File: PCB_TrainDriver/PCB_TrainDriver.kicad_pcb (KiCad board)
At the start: 2 copper layers, 1 part, among them Q1 BSC014N04LS

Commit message: Finished sch
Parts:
- added C1: 1uF 25V, Capacitor_SMD:C_0805_2012Metric, F.Cu at (166.2, 71.7)
- added C10: 1uF 25V, Capacitor_SMD:C_0805_2012Metric, F.Cu at (166.2, 86.7)
- added C11: 1000uF 35V, Capacitor_SMD:CP_Elec_10x10, F.Cu at (148.5, 103.0)
- added C12: 0.1uF 50V, Capacitor_SMD:C_0805_2012Metric, F.Cu at (166.2, 89.7)
- added C13: 1uF 25V, Capacitor_SMD:C_0805_2012Metric, F.Cu at (166.2, 92.7)
- added C14: 1000uF 35V, Capacitor_SMD:CP_Elec_10x10, F.Cu at (148.5, 114.9)
- added C15: 0.1uF, Capacitor_SMD:C_0402_1005Metric, F.Cu at (242.8, 50.7)
- added C16: 0.1uF, Capacitor_SMD:C_0402_1005Metric, F.Cu at (242.8, 52.7)
- added C17: 0.1uF, Capacitor_SMD:C_0402_1005Metric, F.Cu at (242.8, 54.6)
- added C18: 0.1uF, Capacitor_SMD:C_0402_1005Metric, F.Cu at (242.8, 56.6)
- added C19: 10uF, Capacitor_SMD:C_0402_1005Metric, F.Cu at (242.8, 58.6)
- added C2: 0.1uF 50V, Capacitor_SMD:C_0805_2012Metric, F.Cu at (166.2, 74.7)
- added C20: 10uF, Capacitor_SMD:C_1206_3216Metric, F.Cu at (224.8, 118.9)
- added C21: 0.1uF, Capacitor_SMD:C_0603_1608Metric, F.Cu at (212.6, 133.4)
- added C22: 33nF, Capacitor_SMD:C_0402_1005Metric, F.Cu at (216.8, 118.2)
- added C23: 18pF, Capacitor_SMD:C_0402_1005Metric, F.Cu at (216.8, 120.2)
- added C24: 47uF, Capacitor_SMD:C_1206_3216Metric, F.Cu at (224.8, 122.2)
- added C25: 0.1uF, Capacitor_SMD:C_0402_1005Metric, F.Cu at (216.8, 122.1)
- added C26: 1uF, Capacitor_SMD:C_0402_1005Metric, F.Cu at (216.8, 124.1)
- added C27: 220uF, Capacitor_SMD:C_1206_3216Metric, F.Cu at (224.8, 125.6)
- added C28: 0.1uF, Capacitor_SMD:C_0402_1005Metric, F.Cu at (216.8, 126.1)
- added C29: 0.1uF, Capacitor_SMD:C_0402_1005Metric, F.Cu at (242.8, 60.5)
- added C3: 1uF 25V, Capacitor_SMD:C_0805_2012Metric, F.Cu at (166.2, 77.7)
- added C30: 1uF, Capacitor_SMD:C_0402_1005Metric, F.Cu at (242.8, 62.5)
- added C31: 1uF, Capacitor_SMD:C_0402_1005Metric, F.Cu at (216.8, 128.1)
- added C32: 0.1uF, Capacitor_SMD:C_0402_1005Metric, F.Cu at (216.8, 130.0)
- added C4: 1uF 25V, Capacitor_SMD:C_0805_2012Metric, F.Cu at (166.2, 80.7)
- added C5: 1000uF 35V, Capacitor_SMD:CP_Elec_10x10, F.Cu at (148.5, 55.6)
- added C6: 1000uF 35V, Capacitor_SMD:CP_Elec_10x10, F.Cu at (148.5, 67.5)
- added C7: 1000uF 35V, Capacitor_SMD:CP_Elec_10x10, F.Cu at (148.5, 79.3)
- added C8: 1000uF 35V, Capacitor_SMD:CP_Elec_10x10, F.Cu at (148.5, 91.2)
- added C9: 1uF 25V, Capacitor_SMD:C_0805_2012Metric, F.Cu at (166.2, 83.7)
- added CN1: XT90PW-M.G.Y, Sharing_Footprint:CONN-TH_XT90PW-M.G.Y, F.Cu at (86.2, 76.9)
- added D1: SS34, Diode_SMD:D_SMA, F.Cu at (158.0, 142.0)
- added D2: SS34, Diode_SMD:D_SMA, F.Cu at (158.0, 146.5)
- added D3: SS34, Diode_SMD:D_SMA, F.Cu at (158.0, 151.1)
- added D6: LED, LED_SMD:LED_0402_1005Metric, F.Cu at (227.9, 136.9)
- added J1: Motor1_OUT, Connector_AMASS:AMASS_XT60PW-M_1x02_P7.20mm_Horizontal, F.Cu at (160.4, 67.1)
- added J2: Motor2_OUT, Connector_AMASS:AMASS_XT60PW-M_1x02_P7.20mm_Horizontal, F.Cu at (178.0, 67.1)
- added J3: aux_port1, Connector_AMASS:AMASS_XT30PW-M_1x02_P2.50mm_Horizontal, F.Cu at (151.3, 136.9)
- added J4: aux_port2, Connector_AMASS:AMASS_XT30PW-M_1x02_P2.50mm_Horizontal, F.Cu at (166.7, 136.9)
- added J5: aux_port3, Connector_AMASS:AMASS_XT30PW-M_1x02_P2.50mm_Horizontal, F.Cu at (182.0, 136.9)
- added L1: 10uH 21mOhms, Inductor_SMD:L_12x12mm_H4.5mm, F.Cu at (222.7, 110.1)
- added Q10: BSC014N04LS, Package_SON:Infineon_PG-TDSON-8_6.15x5.15mm, F.Cu at (145.7, 149.7)
- added Q11: BSC014N04LS, Package_SON:Infineon_PG-TDSON-8_6.15x5.15mm, F.Cu at (145.7, 156.4)
- added Q12: SS8050, Package_TO_SOT_SMD:SOT-23, F.Cu at (216.2, 94.2)
- added Q13: SS8050, Package_TO_SOT_SMD:SOT-23, F.Cu at (216.2, 98.6)
- added Q2: BSC014N04LS, Package_SON:Infineon_PG-TDSON-8_6.15x5.15mm, F.Cu at (159.8, 73.5)
- added Q3: BSC014N04LS, Package_SON:Infineon_PG-TDSON-8_6.15x5.15mm, F.Cu at (159.8, 80.2)
- added Q4: BSC014N04LS, Package_SON:Infineon_PG-TDSON-8_6.15x5.15mm, F.Cu at (159.8, 86.9)
- added Q5: BSC014N04LS, Package_SON:Infineon_PG-TDSON-8_6.15x5.15mm, F.Cu at (159.8, 93.6)
- added Q6: BSC014N04LS, Package_SON:Infineon_PG-TDSON-8_6.15x5.15mm, F.Cu at (159.8, 100.3)
- added Q7: BSC014N04LS, Package_SON:Infineon_PG-TDSON-8_6.15x5.15mm, F.Cu at (159.8, 106.9)
- added Q8: BSC014N04LS, Package_SON:Infineon_PG-TDSON-8_6.15x5.15mm, F.Cu at (159.8, 113.6)
- added Q9: BSC014N04LS, Package_SON:Infineon_PG-TDSON-8_6.15x5.15mm, F.Cu at (145.7, 143.0)
- added R1: 33k, Resistor_SMD:R_0603_1608Metric, F.Cu at (177.1, 71.4)
- added R10: 10k, Resistor_SMD:R_0603_1608Metric, F.Cu at (151.9, 148.5)
- added R11: 330, Resistor_SMD:R_0603_1608Metric, F.Cu at (151.9, 151.0)
- added R12: 10k, Resistor_SMD:R_0603_1608Metric, F.Cu at (151.9, 153.5)
- added R13: 5.1k, Resistor_SMD:R_0402_1005Metric, F.Cu at (242.8, 64.5)
- added R14: 5.1k, Resistor_SMD:R_0402_1005Metric, F.Cu at (242.8, 66.5)
- added R15: 10k, Resistor_SMD:R_0402_1005Metric, F.Cu at (242.8, 68.5)
- added R16: 10k, Resistor_SMD:R_0402_1005Metric, F.Cu at (242.8, 70.5)
- added R17: 10k, Resistor_SMD:R_0402_1005Metric, F.Cu at (242.8, 72.4)
- added R18: 0.25mOhms 15W, Sharing_Footprint:R5930, F.Cu at (201.5, 137.5)
- added R2: 10k, Resistor_SMD:R_0603_1608Metric, F.Cu at (177.1, 73.9)
- added R23: 52.3k, Resistor_SMD:R_0603_1608Metric, F.Cu at (212.6, 135.9)
- added R24: 10k, Resistor_SMD:R_0402_1005Metric, F.Cu at (219.7, 136.9)
- added R25: 4.7k, Resistor_SMD:R_0402_1005Metric, F.Cu at (219.7, 138.9)
- added R26: 4.7k, Resistor_SMD:R_0402_1005Metric, F.Cu at (219.7, 140.9)
- added R3: 68k, Resistor_SMD:R_0603_1608Metric, F.Cu at (177.1, 76.4)
- added R4: 10k, Resistor_SMD:R_0603_1608Metric, F.Cu at (177.1, 78.9)
- added R5: 68k, Resistor_SMD:R_0603_1608Metric, F.Cu at (177.1, 81.4)
- added R6: 33k, Resistor_SMD:R_0603_1608Metric, F.Cu at (177.1, 84.0)
- added R7: 10k, Resistor_SMD:R_0603_1608Metric, F.Cu at (151.9, 141.0)
- added R8: 330, Resistor_SMD:R_0603_1608Metric, F.Cu at (151.9, 143.5)
- added R9: 330, Resistor_SMD:R_0603_1608Metric, F.Cu at (151.9, 146.0)
- added SW1: SW_Push, Button_Switch_SMD:SW_Tactile_SPST_NO_Straight_CK_PTS636Sx25SMTRLFS, F.Cu at (208.5, 94.6)
- added TP1: VCC, Connector_Pin:Pin_D0.7mm_L6.5mm_W1.8mm_FlatFork, F.Cu at (220.1, 118.9)
- added TP2: 5V, Connector_Pin:Pin_D0.7mm_L6.5mm_W1.8mm_FlatFork, F.Cu at (220.1, 122.4)
- added TP3: +3.3V, Connector_Pin:Pin_D0.7mm_L6.5mm_W1.8mm_FlatFork, F.Cu at (220.1, 125.8)
- added U1: DRV8701ERGER, Package_DFN_QFN:VQFN-24-1EP_4x4mm_P0.5mm_EP2.45x2.45mm, F.Cu at (172.0, 73.3)
- added U2: DRV8701ERGER, Package_DFN_QFN:VQFN-24-1EP_4x4mm_P0.5mm_EP2.45x2.45mm, F.Cu at (172.0, 79.6)
- added U3: ESP32-S3-WROOM-1, RF_Module:ESP32-S3-WROOM-1, F.Cu at (101.8, 138.2)
- added U4: TPS62932, Package_TO_SOT_SMD:SOT-583-8, F.Cu at (212.4, 139.2)
- added U5: CH343P, Package_DFN_QFN:WCH_QFN-16-1EP_3x3mm_P0.5mm_EP1.8x1.8mm, F.Cu at (221.7, 94.6)
- added U6: INA219AxDCN, Package_TO_SOT_SMD:SOT-23-8, F.Cu at (223.7, 138.3)
- added U7: USBLC6-2P6, Package_TO_SOT_SMD:SOT-666, F.Cu at (220.7, 99.1)
- added U9: LDL1117S33R, Package_TO_SOT_SMD:SOT-223-3_TabPin2, F.Cu at (223.1, 131.8)
- added USB1: USB-C 16 Pins, Sharing_Footprint:USB-C-SMD_TYPE-C-16PIN, F.Cu at (197.8, 95.4)
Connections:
- net Net-(Q1-S-Pad1) renamed /H-Bridge_Driver/SH1_1
- Q1 pad 4: unconnected-(Q1-G-Pad4) -> /H-Bridge_Driver/GH1_1
- Q1 pad 5: unconnected-(Q1-D-Pad5) -> +12V
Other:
- board outline added: 6.5 x 0.7 mm

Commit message: PCB Almost Finished
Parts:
- added D10: LED, LED_SMD:LED_0603_1608Metric, F.Cu at (200.3, 57.9)
- added D11: LED, LED_SMD:LED_0603_1608Metric, F.Cu at (202.8, 57.9)
- added D12: LED, LED_SMD:LED_0603_1608Metric, F.Cu at (205.3, 57.9)
- added D4: BAT54S, Package_TO_SOT_SMD:SOT-23, F.Cu at (192.0, 55.2)
- added D9: LED, LED_SMD:LED_0603_1608Metric, F.Cu at (197.8, 57.8)
- added H1: MountingHole, MountingHole:MountingHole_5.3mm_M5_DIN965_Pad, F.Cu at (55.0, 137.0)
- added H2: MountingHole, MountingHole:MountingHole_5.3mm_M5_DIN965_Pad, F.Cu at (251.0, 137.0)
- added H3: MountingHole, MountingHole:MountingHole_5.3mm_M5_DIN965_Pad, F.Cu at (55.0, 47.0)
- added H4: MountingHole, MountingHole:MountingHole_5.3mm_M5_DIN965_Pad, F.Cu at (166.0, 98.0)
- added H5: MountingHole, MountingHole:MountingHole_5.3mm_M5_DIN965_Pad, F.Cu at (218.0, 58.0)
- added J6: JoyStickConnector, Connector_JST:JST_XH_B7B-XH-A_1x07_P2.50mm_Vertical, F.Cu at (195.3, 45.4)
- added R19: 33k, Resistor_SMD:R_0603_1608Metric, F.Cu at (194.5, 52.2)
- added R20: 10k, Resistor_SMD:R_0603_1608Metric, F.Cu at (204.1, 72.5)
- added R21: 10k, Resistor_SMD:R_0603_1608Metric, F.Cu at (201.6, 72.5)
- added R22: 10k, Resistor_SMD:R_0603_1608Metric, F.Cu at (199.1, 72.3)
- added R27: 1k, Resistor_SMD:R_0402_1005Metric, F.Cu at (58.0, 77.4)
- added R28: 10k, Resistor_SMD:R_0603_1608Metric, F.Cu at (191.2, 52.2)
- added R29: 10k, Resistor_SMD:R_0603_1608Metric, F.Cu at (196.4, 72.3)
- added R30: 22k, Resistor_SMD:R_1206_3216Metric, F.Cu at (197.8, 53.8)
- added R31: 22k, Resistor_SMD:R_1206_3216Metric, F.Cu at (200.3, 53.8)
- added R32: 22k, Resistor_SMD:R_1206_3216Metric, F.Cu at (202.8, 53.8)
- added R33: 22k, Resistor_SMD:R_1206_3216Metric, F.Cu at (205.3, 53.8)
- added U8: TLP291-4, Package_SO:SOIC-16_4.55x10.3mm_P1.27mm, F.Cu at (200.9, 65.7)
- C15, C16, C17, C18, C21, C25, C28, C29, C32: value 0.1uF -> 0.1uF 50V
- C19: value 10uF -> 10uF 10V
- C20: value 10uF -> 10uF 50V
- C22: value 33nF -> 33nF 10V
- C23: value 18pF -> 18pF 25V
- C24: value 47uF -> 47uF 16V
- D6: footprint LED_SMD:LED_0402_1005Metric -> LED_SMD:LED_0603_1608Metric
- moved D6 180.6 mm to (58.0, 76.0)
- moved U9 177.6 mm to (59.0, 64.0), turned to 90 degrees
- moved C27 175.1 mm to (57.9, 72.7), turned to 180 degrees
- moved C24 169.1 mm to (64.2, 69.3), turned to 90 degrees
- moved C26 167.7 mm to (57.8, 70.7), turned to 180 degrees
- moved C25 167.5 mm to (57.8, 69.5), turned to 180 degrees
- moved C31 166.1 mm to (61.2, 69.6), turned to -90 degrees
- moved TP3 164.3 mm to (63.5, 76.0)
- moved L1 155.8 mm to (73.3, 66.1), turned to 180 degrees
- moved U6 150.8 mm to (86.5, 75.8), turned to 90 degrees
- moved R24 149.8 mm to (85.7, 69.9), turned to 180 degrees
- moved R25 148.2 mm to (87.4, 72.0), turned to 180 degrees
- moved R26 148.0 mm to (88.0, 73.3), turned to 180 degrees
- moved TP2 146.7 mm to (82.3, 72.2)
- moved C28 146.2 mm to (83.3, 66.2), turned to 90 degrees
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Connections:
- J1 pad 1: /H-Bridge_Driver/SH1_1 -> /H-Bridge_Driver/SH2_1
- J1 pad 2: /H-Bridge_Driver/SH2_1 -> /H-Bridge_Driver/SH1_1
- J2 pad 1: /H-Bridge_Driver/SH1_2 -> /H-Bridge_Driver/SH2_2
- J2 pad 2: /H-Bridge_Driver/SH2_2 -> /H-Bridge_Driver/SH1_2
- U1 pad 17: /H-Bridge_Driver/GL1_1 -> /H-Bridge_Driver/GH1_1
- U1 pad 19: /H-Bridge_Driver/GH1_1 -> /H-Bridge_Driver/GL1_1
- U2 pad 17: /H-Bridge_Driver/GL1_2 -> /H-Bridge_Driver/GH1_2
- U2 pad 19: /H-Bridge_Driver/GH1_2 -> /H-Bridge_Driver/GL1_2
- U3 pad 12: /H-Bridge_Driver/EN_2 -> /H-Bridge_Driver/nFAULT_1
- U3 pad 16: unconnected-(U3-IO46-Pad16) -> /MCU/BackwardIN_3.3V
- U3 pad 18: /H-Bridge_Driver/nSLEEP_2 -> /H-Bridge_Driver/EN_2
- U3 pad 19: /H-Bridge_Driver/nFAULT_2 -> /H-Bridge_Driver/nSLEEP_2
- U3 pad 20: /MCU/Pneumatic -> /H-Bridge_Driver/nFAULT_2
- U3 pad 21: /MCU/Horn -> /MCU/Lamp
- U3 pad 22: /MCU/Lamp -> /MCU/Horn
- U3 pad 23: unconnected-(U3-IO21-Pad23) -> /MCU/Pneumatic
- U3 pad 24: unconnected-(U3-IO47-Pad24) -> /MCU/HornIN_3.3V
- U3 pad 25: unconnected-(U3-IO48-Pad25) -> /MCU/LampIN_3.3V
- U3 pad 35: unconnected-(U3-IO42-Pad35) -> /MCU/ForwardIN_3.3V
- U3 pad 4: /H-Bridge_Driver/EN_1 -> /MCU/Speed_ControlIN_3.3V
- U3 pad 6: /H-Bridge_Driver/nSLEEP_1 -> /H-Bridge_Driver/EN_1
- U3 pad 7: /H-Bridge_Driver/nFAULT_1 -> /H-Bridge_Driver/nSLEEP_1
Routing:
- net /MCU/Pneumatic: track 0.00 -> 142.7 mm
- net /MCU/Horn: track 0.00 -> 129.8 mm
- net /MCU/Lamp: track 0.00 -> 117.4 mm
- net /H-Bridge_Driver/nFAULT_2: track 0.00 -> 95.1 mm
- net /H-Bridge_Driver/PH_2: track 0.00 -> 94.6 mm
- net /MCU/Speed_ControlIN_3.3V: track 0.00 -> 94.1 mm, vias 0 -> 2
- net /H-Bridge_Driver/EN_2: track 0.00 -> 92.8 mm
- net /H-Bridge_Driver/nSLEEP_2: track 0.00 -> 91.1 mm
- net /MCU/HornIN_3.3V: track 0.00 -> 86.9 mm
- net /MCU/BackwardIN_3.3V: track 0.00 -> 83.5 mm, vias 0 -> 2
- net /MCU/LampIN_3.3V: track 0.00 -> 80.9 mm
- net GND: track 0.00 -> 79.4 mm, vias 0 -> 696
- net /MCU/ForwardIN_3.3V: track 0.00 -> 72.1 mm
- net /H-Bridge_Driver/GH2_2: track 0.00 -> 70.9 mm
- net /H-Bridge_Driver/GH2_1: track 0.00 -> 68.9 mm
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- added copper zone on F.Cu, net +12V
- added copper zone on In2.Cu, net +12V
- added copper zone on F.Cu, net +3.3V
- added copper zone on In2.Cu, net +3.3V
- added copper zone on F.Cu, net +5V
- added copper zone on B.Cu, net /H-Bridge_Driver/SH1_1
- added copper zone on F.Cu, net /H-Bridge_Driver/SH1_1
- added copper zone on B.Cu, net /H-Bridge_Driver/SH1_2
- added copper zone on F.Cu, net /H-Bridge_Driver/SH1_2
- added copper zone on B.Cu, net /H-Bridge_Driver/SH2_1
- added copper zone on F.Cu, net /H-Bridge_Driver/SH2_1
- added copper zone on B.Cu, net /H-Bridge_Driver/SH2_2
- added copper zone on F.Cu, net /H-Bridge_Driver/SH2_2
- added copper zone on B.Cu, net GND
- added copper zone on F.Cu, net GND
- added copper zone on In1.Cu, net GND
- added copper zone on F.Cu, net Net-(D1-A)
- added copper zone on F.Cu, net Net-(D2-A)
- added copper zone on F.Cu, net Net-(D3-A)
- added copper zone on F.Cu, net Net-(U4-SW)
- added copper zone on F.Cu, net VCC
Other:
- board size 6.5 x 0.7 mm -> 208.5 x 102.3 mm
- copper layers 2 -> 4
- board text added: "Q1"

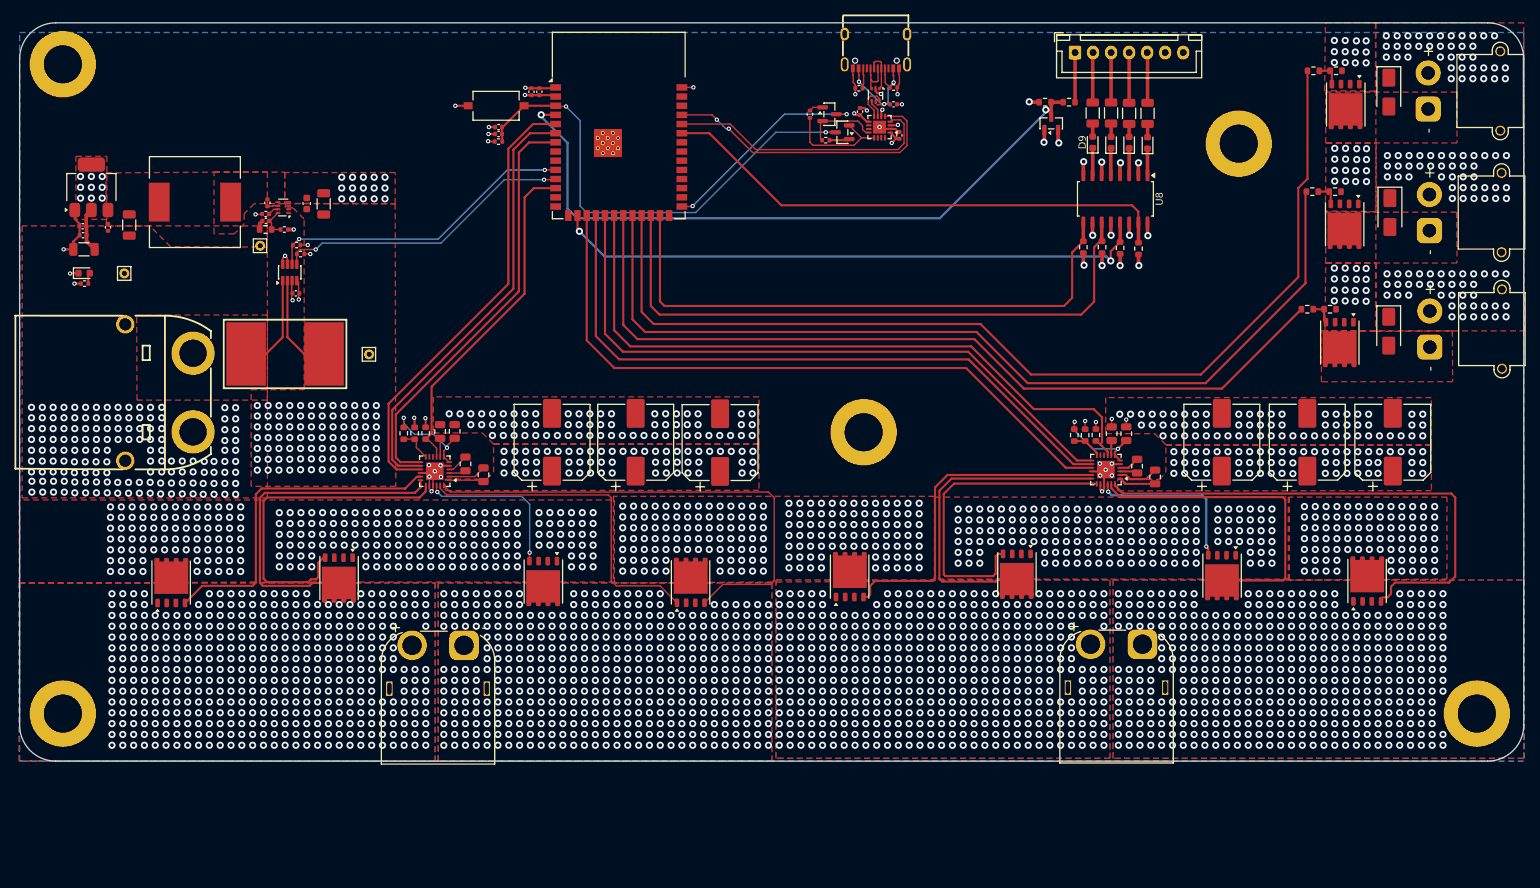
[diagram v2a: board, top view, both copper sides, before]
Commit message: Add aux led indicator
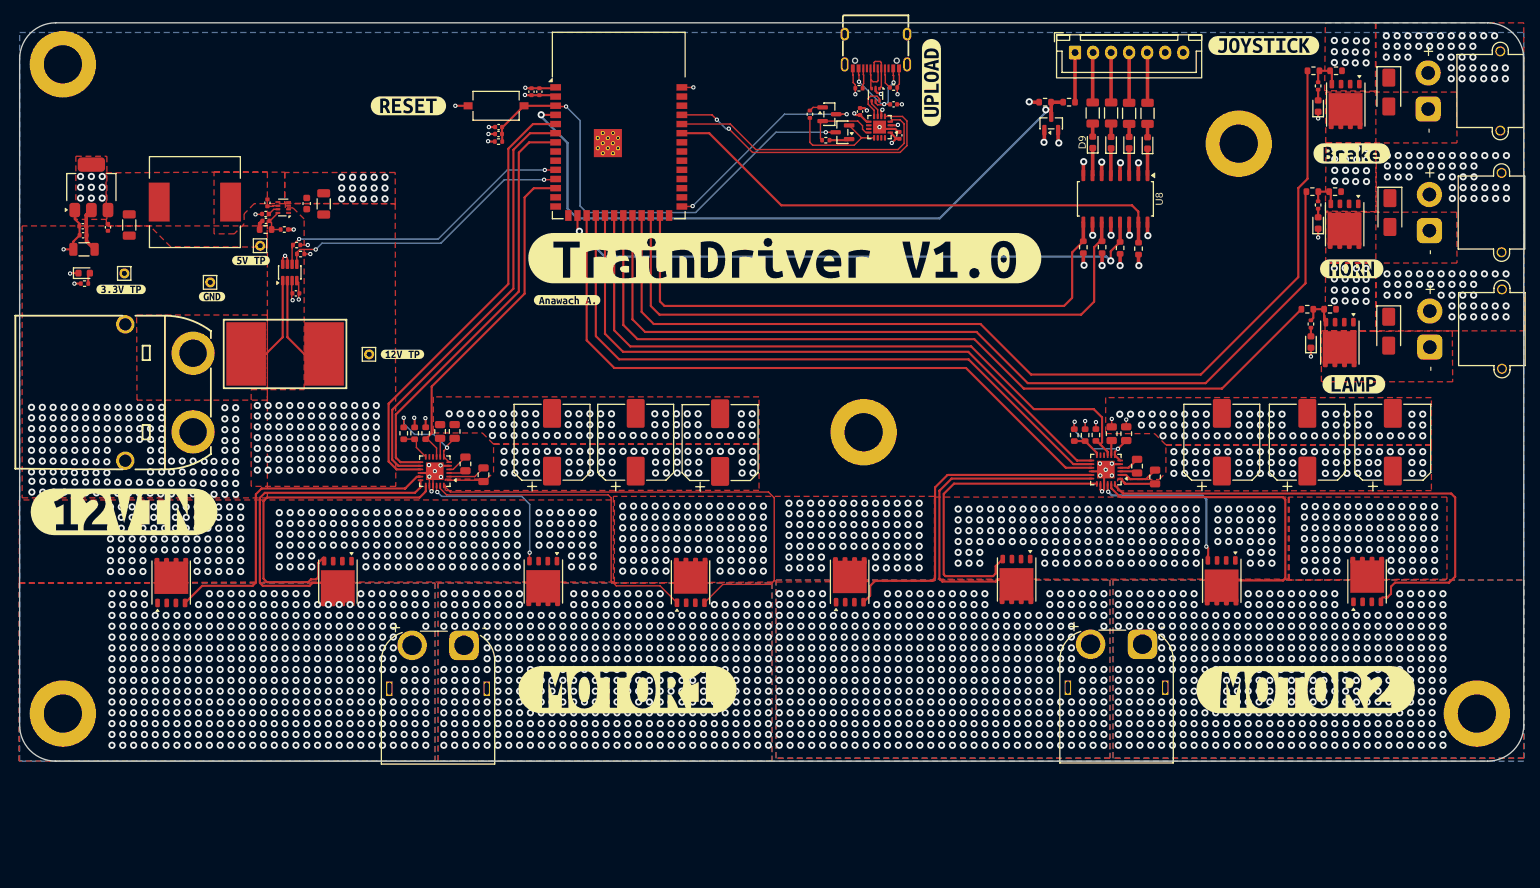
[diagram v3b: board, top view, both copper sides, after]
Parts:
- added D13: LED, LED_SMD:LED_0603_1608Metric, F.Cu at (229.0, 52.8)
- added D7: LED, LED_SMD:LED_0603_1608Metric, F.Cu at (228.0, 85.5)
- added D8: LED, LED_SMD:LED_0603_1608Metric, F.Cu at (229.0, 69.0)
- added R34: 1k, Resistor_SMD:R_0402_1005Metric, F.Cu at (228.0, 83.0)
- added R35: 1k, Resistor_SMD:R_0402_1005Metric, F.Cu at (229.0, 66.5)
- added R36: 1k, Resistor_SMD:R_0402_1005Metric, F.Cu at (229.0, 50.0)
- added TP4: GND, Connector_Pin:Pin_D0.7mm_L6.5mm_W1.8mm_FlatFork, F.Cu at (75.4, 77.2)
- added kibuzzard-6A412E14: G***, kibuzzard-6A412E14, F.Cu at (133.3, 133.7)
- added kibuzzard-6A412E20: G***, kibuzzard-6A412E20, F.Cu at (227.3, 133.7)
- added kibuzzard-6A412E33: G***, kibuzzard-6A412E33, F.Cu at (63.5, 109.0)
- added kibuzzard-6A412E56: G***, kibuzzard-6A412E56, F.Cu at (102.9, 52.8)
- added kibuzzard-6A412E6E: G***, kibuzzard-6A412E6E, F.Cu at (221.5, 44.4)
- added kibuzzard-6A412E9B: G***, kibuzzard-6A412E9B, F.Cu at (234.0, 91.4)
- added kibuzzard-6A412EAB: G***, kibuzzard-6A412EAB, F.Cu at (233.7, 75.4)
- added kibuzzard-6A412ECC: G***, kibuzzard-6A412ECC, F.Cu at (233.7, 59.4)
- added kibuzzard-6A412EE2: G***, kibuzzard-6A412EE2, F.Cu at (175.4, 49.5)
- added kibuzzard-6A412F0B: G***, kibuzzard-6A412F0B, F.Cu at (155.1, 73.9)
- added kibuzzard-6A412F26: G***, kibuzzard-6A412F26, F.Cu at (124.9, 79.7)
- added kibuzzard-6A412FC6: G***, kibuzzard-6A412FC6, F.Cu at (102.1, 87.2)
- added kibuzzard-6A412FD5: G***, kibuzzard-6A412FD5, F.Cu at (81.1, 74.2)
- added kibuzzard-6A412FE5: G***, kibuzzard-6A412FE5, F.Cu at (63.1, 78.2)
- added kibuzzard-6A412FEF: G***, kibuzzard-6A412FEF, F.Cu at (75.7, 79.2)
- moved Q6 0.72 mm to (187.2, 118.4)
- moved Q5 0.72 mm to (164.1, 118.7)
- moved Q8 0.72 mm to (215.6, 118.6)
- moved Q2 0.50 mm to (93.1, 118.7)
- moved Q7 0.06 mm to (235.8, 118.7)
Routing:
- net GND: track 79.4 -> 82.8 mm, vias 696 -> 699
- net Net-(Q11-G): track 3.40 -> 5.08 mm
- net Net-(Q9-G): track 3.43 -> 5.10 mm
- net Net-(D13-A): track 0.00 -> 1.49 mm
- net Net-(Q10-G): track 3.29 -> 4.64 mm
- net /H-Bridge_Driver/GL1_2: track 44.2 -> 43.0 mm
- net Net-(D8-A): track 0.00 -> 1.20 mm
- net Net-(D7-A): track 0.00 -> 1.20 mm
- net /H-Bridge_Driver/GL2_2: track 23.1 -> 23.8 mm
- net /H-Bridge_Driver/SH1_2: vias 438 -> 431
